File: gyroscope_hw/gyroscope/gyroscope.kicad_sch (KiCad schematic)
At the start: 56 parts, among them Q1 YJL2305A, Q2 LED_5050, Q3 YJL2305A, U1 STM32F103C8Tx

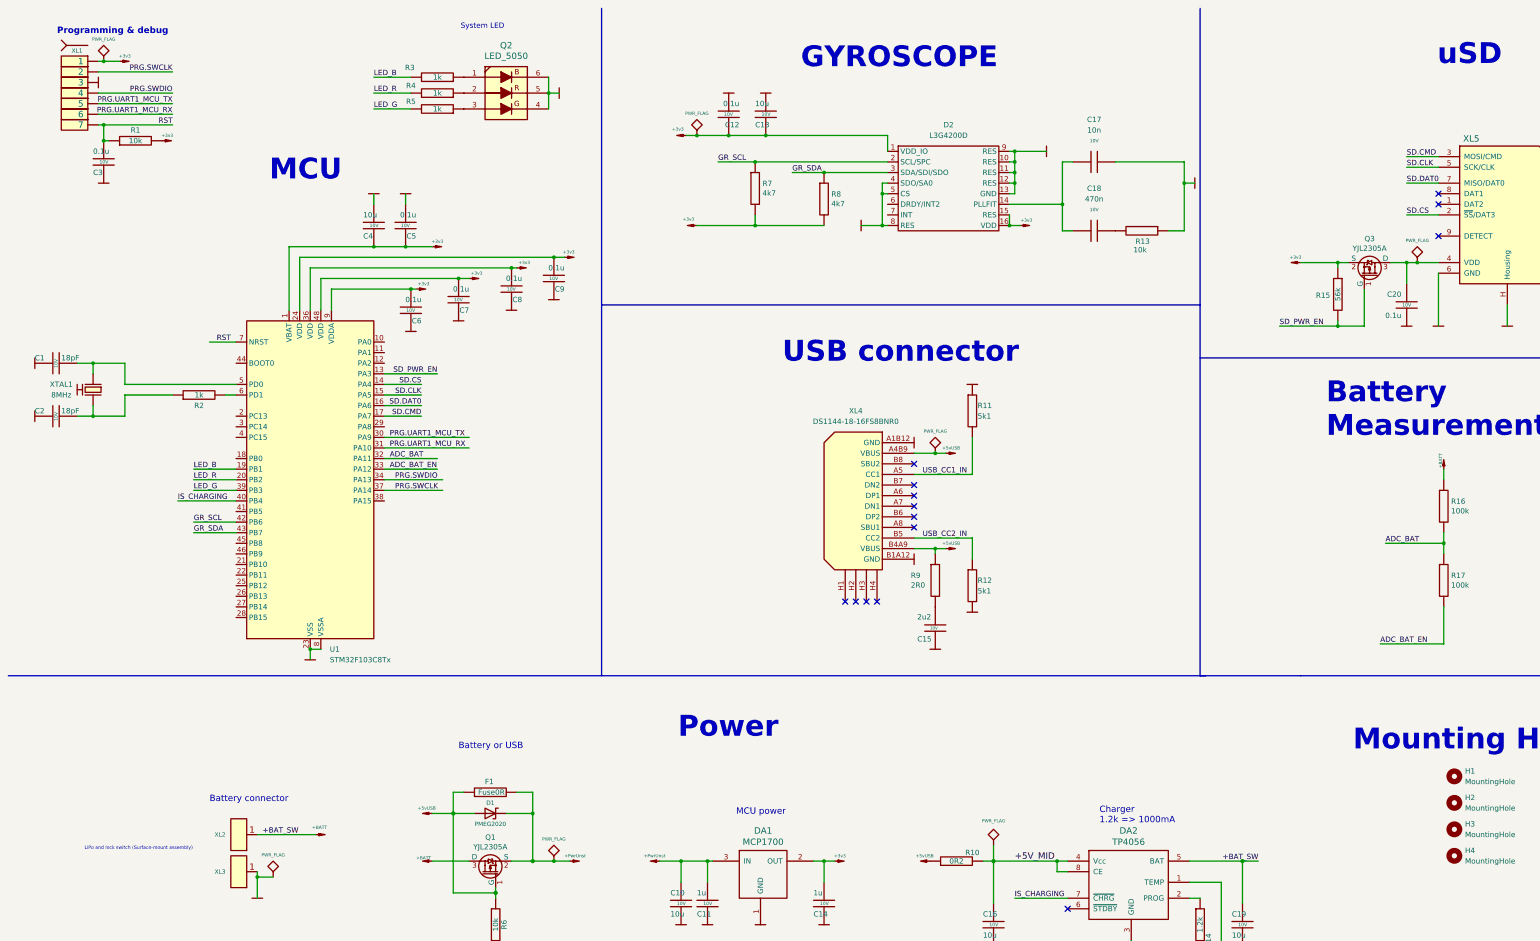
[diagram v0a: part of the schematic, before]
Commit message: Added firmware and correct PCB
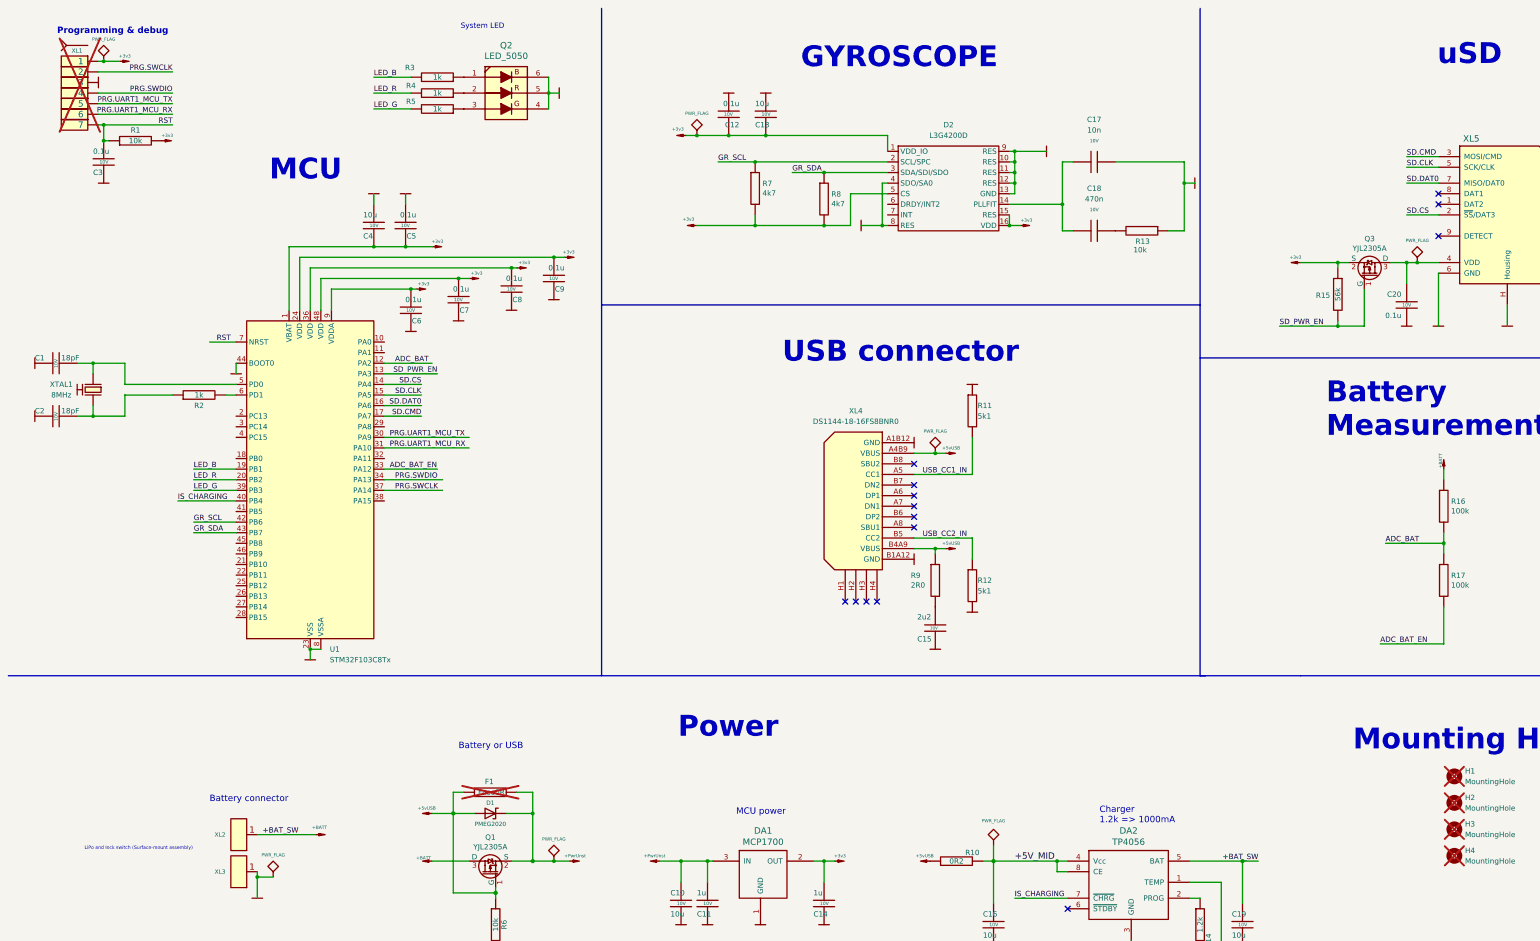
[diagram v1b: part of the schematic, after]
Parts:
- F1, H1, H2, H3, H4, XL1: now not fitted
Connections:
- net +3v3: now also D2.5 (CS)
- net ADC_BAT: now also U1.12 (PA2); no longer U1.32 (PA11)
- net GND: now also U1.44 (BOOT0); no longer D2.5 (CS)
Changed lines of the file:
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@@
 	)
 	(junction
-		(at 222.25 57.15)
-		(diameter 0)
-		(color 0 0 0 0)
-	)
-	(junction
 		(at 35.56 25.4)
 		(diameter 0)
@@
 	)
 	(junction
+		(at 208.28 64.77)
+		(diameter 0)
+		(color 0 0 0 0)
+	)
+	(junction
 		(at 356.87 140.97)
 		(diameter 0)
@@
 	(wire
 		(pts
-			(xy 223.52 57.15) (xy 222.25 57.15)
-		)
-		(stroke
-			(width 0)
-			(type default)
-		)
-	)
-	(wire
-		(pts
 			(xy 142.24 33.02) (xy 142.24 36.83)
 		)
@@
 	(wire
 		(pts
+			(xy 102.87 97.79) (xy 114.3 97.79)
+		)
+		(stroke
+			(width 0)
+			(type default)
+		)
+	)
+	(wire
+		(pts
 			(xy 143.51 217.17) (xy 147.32 217.17)
 		)
@@
 	(wire
 		(pts
-			(xy 222.25 57.15) (xy 222.25 64.77)
+			(xy 222.25 54.61) (xy 222.25 64.77)
 		)
 		(stroke
@@
 		)
 	)
-	(wire
-		(pts
-			(xy 222.25 54.61) (xy 222.25 57.15)
-		)
-		(stroke
-			(width 0)
-			(type default)
-		)
-	)
 	(polyline
 		(pts
@@
 	(wire
 		(pts
-			(xy 102.87 120.65) (xy 115.57 120.65)
-		)
-		(stroke
-			(width 0)
-			(type default)
-		)
-	)
-	(wire
-		(pts
 			(xy 114.3 205.74) (xy 119.38 205.74)
 		)
@@
 	(wire
 		(pts
+			(xy 67.31 97.79) (xy 67.31 100.33)
+		)
+		(stroke
+			(width 0)
+			(type default)
+		)
+	)
+	(wire
+		(pts
 			(xy 356.87 140.97) (xy 356.87 138.43)
 		)
@@
 	(wire
 		(pts
+			(xy 214.63 57.15) (xy 214.63 64.77)
+		)
+		(stroke
+			(width 0)
+			(type default)
+		)
+	)
+	(wire
+		(pts
 			(xy 356.87 156.21) (xy 356.87 165.1)
 		)
@@
 	(wire
 		(pts
+			(xy 214.63 64.77) (xy 208.28 64.77)
+		)
+		(stroke
+			(width 0)
+			(type default)
+		)
+	)
+	(wire
+		(pts
 			(xy 252.73 46.99) (xy 254 46.99)
 		)
@@
 	(wire
 		(pts
+			(xy 223.52 57.15) (xy 214.63 57.15)
+		)
+		(stroke
+			(width 0)
+			(type default)
+		)
+	)
+	(wire
+		(pts
 			(xy 234.95 142.24) (xy 234.95 143.51)
 		)
@@
 		)
 	)
-	(label "ADC_BAT"
-		(at 104.14 120.65 0)
-		(effects
-			(font
-				(size 1.27 1.27)
-			)
-			(justify left bottom)
-		)
-	)
 	(label "PRG.UART1_MCU_RX"
 		(at 52.07 38.1 180)
@@
 		)
 	)
+	(label "ADC_BAT"
+		(at 105.41 97.79 0)
+		(effects
+			(font
+				(size 1.27 1.27)
+			)
+			(justify left bottom)
+		)
+	)
 	(label "SD_PWR_EN"
 		(at 317.5 88.9 0)
@@
 		(in_bom no)
 		(on_board yes)
-		(dnp no)
+		(dnp yes)
 		(fields_autoplaced yes)
 		(property "Reference" "H3"
@@
 		(in_bom no)
 		(on_board yes)
-		(dnp no)
+		(dnp yes)
 		(property "Reference" "XL1"
 			(at 30.48 22.86 0)
@@
 		(in_bom no)
 		(on_board yes)
-		(dnp no)
+		(dnp yes)
 		(fields_autoplaced yes)
 		(property "Reference" "H4"
@@
 	(symbol
 		(lib_id "power:GND")
+		(at 67.31 100.33 0)
+		(mirror y)
+		(unit 1)
+		(exclude_from_sim no)
+		(in_bom yes)
+		(on_board yes)
+		(dnp no)
+		(property "Reference" "#PWR059"
+			(at 65.024 100.838 0)
+			(effects
+				(font
+					(size 0.762 0.762)
+				)
+				(hide yes)
+			)
+		)
+		(property "Value" "GND"
+			(at 67.31 102.362 0)
+			(effects
+				(font
+					(size 0.762 0.762)
+				)
+				(hide yes)
+			)
+		)
+		(property "Footprint" ""
+			(at 67.31 100.33 0)
+			(effects
+				(font
+					(size 1.524 1.524)
+				)
+			)
+		)
+		(property "Datasheet" ""
+			(at 67.31 100.33 0)
+			(effects
+				(font
+					(size 1.524 1.524)
+				)
+			)
+		)
+		(property "Description" ""
+			(at 67.31 100.33 0)
+			(effects
+				(font
+					(size 1.27 1.27)
+				)
+				(hide yes)
+			)
+		)
+		(pin "1"
+		)
+		(instances
+			(project "gyroscope"
+				(path "/2a836975-6bcc-4c86-8694-c08f5173e410"
+					(reference "#PWR059")
+					(unit 1)
+				)
+			)
+		)
+	)
+	(symbol
+		(lib_id "power:GND")
 		(at 185.42 33.02 0)
 		(unit 1)
@@
 		(in_bom no)
 		(on_board yes)
-		(dnp no)
+		(dnp yes)
 		(property "Reference" "F1"
 			(at 128.016 198.12 90)
@@
 		(in_bom no)
 		(on_board yes)
-		(dnp no)
+		(dnp yes)
 		(fields_autoplaced yes)
 		(property "Reference" "H1"
@@
 		(in_bom no)
 		(on_board yes)
-		(dnp no)
+		(dnp yes)
 		(fields_autoplaced yes)
 		(property "Reference" "H2"
